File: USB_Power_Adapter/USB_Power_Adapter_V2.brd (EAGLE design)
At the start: 37 x 10 mm, 6 parts, among them J1 MICROUSBMICROUSB_THRU, U1 SC189

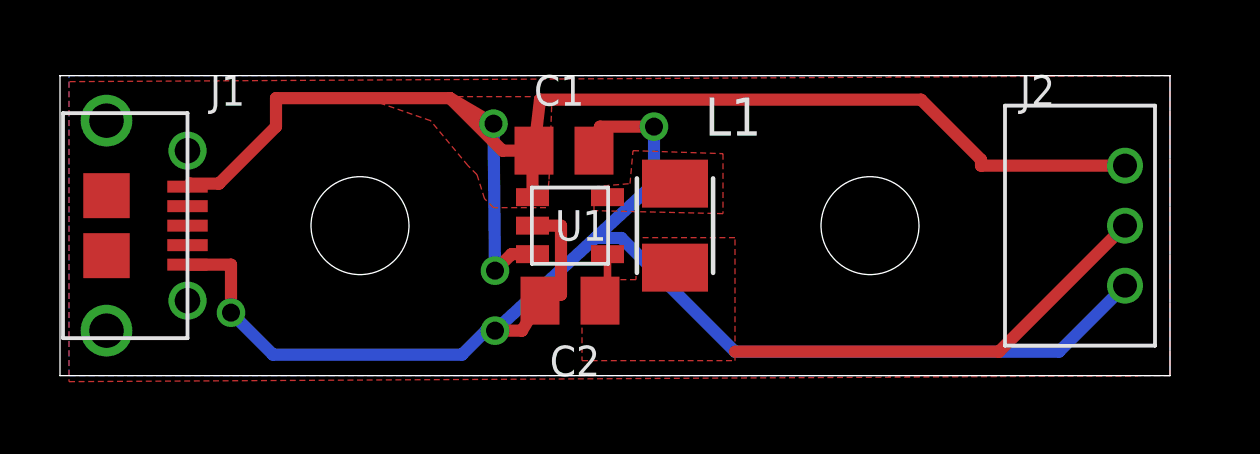
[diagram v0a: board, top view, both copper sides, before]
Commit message: Changed spacing and clearance for USB Power Adapter PCB
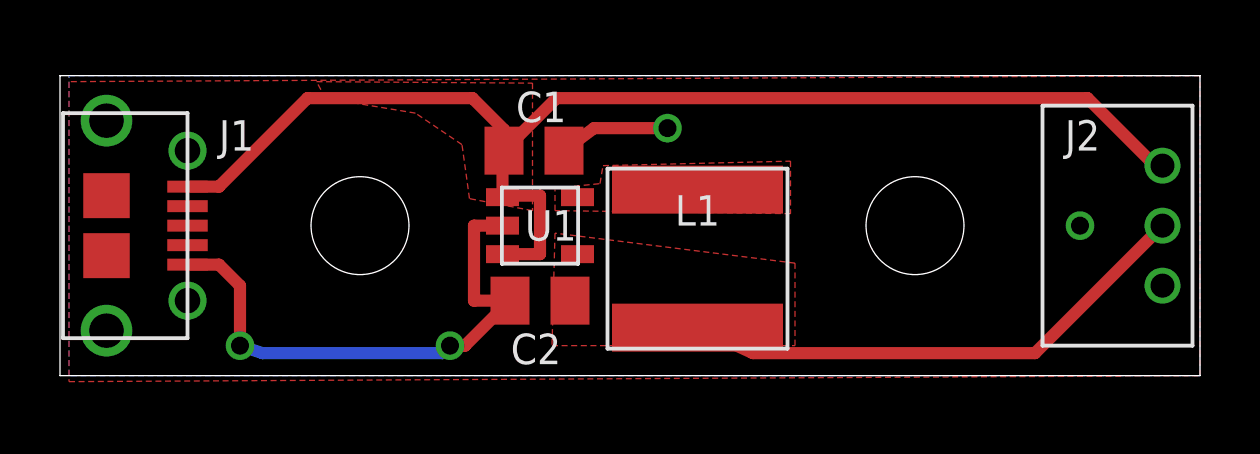
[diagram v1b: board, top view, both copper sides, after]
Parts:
- removed L1: 1uH, resistor:L3225M
- added U$1: SMDINDUCTOR, ScottSilver:SMDINDUCTOR
- moved U$2 1.25 mm to (35.2, 5.00)
- moved C1 1.00 mm to (15.8, 7.50)
- moved C2 1.00 mm to (16.0, 2.50)
- moved U1 1.00 mm to (16.0, 5.00)
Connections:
- net L: now also U$1.P$1; no longer L1.1
- net VOUT: now also U$1.P$2; no longer L1.2
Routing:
- net GND: track 50.9 -> 22.2 mm, vias 3 -> 4
- net VIN: track 46.0 -> 42.6 mm, vias 2 -> 0
- net VOUT: track 16.4 -> 17.4 mm
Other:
- board size 37 x 10 mm -> 38 x 10 mm
- board text added: "L1"
